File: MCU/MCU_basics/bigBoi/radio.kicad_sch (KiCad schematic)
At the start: 23 parts, among them J1 Conn_Coaxial, U1 SX1276, U2 PE4259, Y1 32MHz

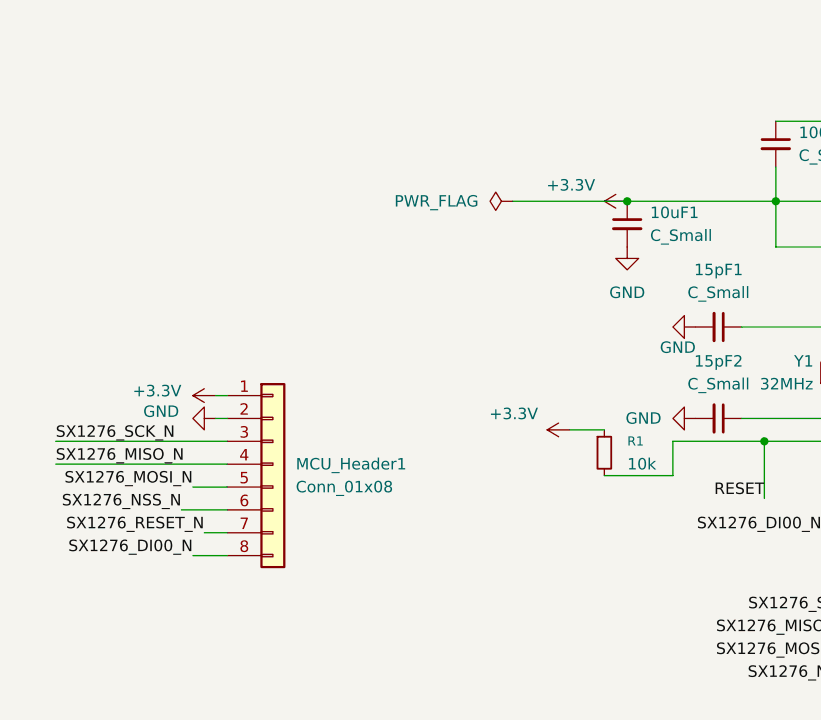
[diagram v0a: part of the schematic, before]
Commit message: Schematic pins assignment
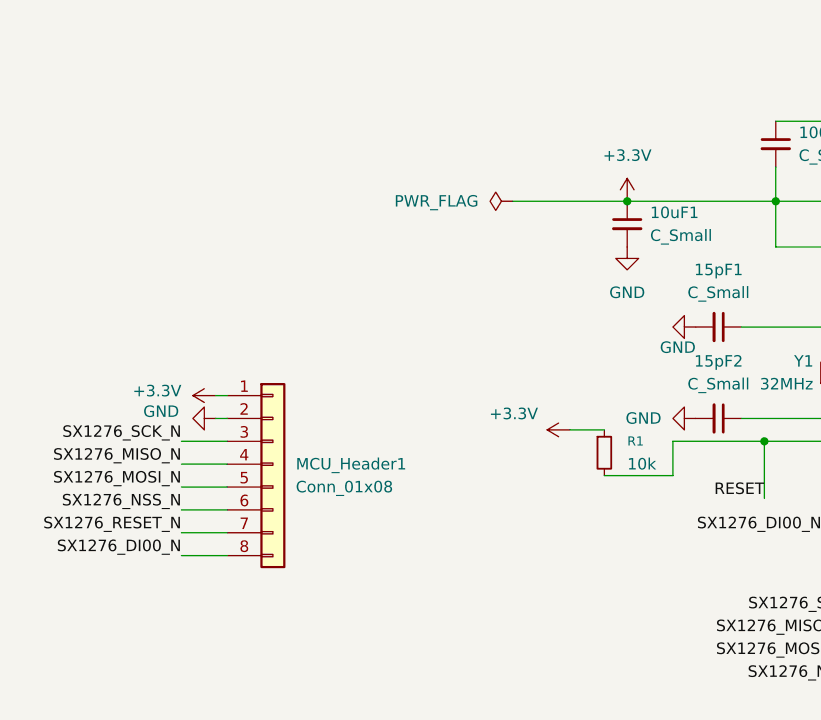
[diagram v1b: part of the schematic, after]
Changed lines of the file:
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@@
 	(wire
 		(pts
-			(xy 48.26 95.25) (xy 52.07 95.25)
+			(xy 46.99 95.25) (xy 52.07 95.25)
 		)
 		(stroke
@@
 	(wire
 		(pts
-			(xy 33.02 92.71) (xy 52.07 92.71)
+			(xy 46.99 92.71) (xy 52.07 92.71)
 		)
 		(stroke
@@
 	(wire
 		(pts
-			(xy 33.02 90.17) (xy 52.07 90.17)
+			(xy 46.99 90.17) (xy 52.07 90.17)
 		)
 		(stroke
@@
 	(wire
 		(pts
-			(xy 48.26 102.87) (xy 52.07 102.87)
+			(xy 46.99 102.87) (xy 52.07 102.87)
 		)
 		(stroke
@@
 	(wire
 		(pts
-			(xy 49.53 100.33) (xy 52.07 100.33)
+			(xy 46.99 100.33) (xy 52.07 100.33)
 		)
 		(stroke
@@
 	)
 	(label "SX1276_MOSI_N"
-		(at 48.26 95.25 180)
+		(at 46.99 95.25 180)
 		(effects
 			(font
@@
 	)
 	(label "SX1276_SCK_N"
-		(at 33.02 90.17 0)
+		(at 46.99 90.17 180)
 		(effects
 			(font
 				(size 1.27 1.27)
 			)
-			(justify left bottom)
+			(justify right bottom)
 		)
 	)
@@
 	)
 	(label "SX1276_DI00_N"
-		(at 48.26 102.87 180)
+		(at 46.99 102.87 180)
 		(effects
 			(font
@@
 	)
 	(label "SX1276_RESET_N"
-		(at 49.53 100.33 180)
+		(at 46.99 100.33 180)
 		(effects
 			(font
@@
 	)
 	(label "SX1276_MISO_N"
-		(at 33.02 92.71 0)
+		(at 46.99 92.71 180)
 		(effects
 			(font
 				(size 1.27 1.27)
 			)
-			(justify left bottom)
+			(justify right bottom)
 		)
 	)
@@
 	)
 	(symbol
+		(lib_id "power:+3.3V")
+		(at 96.52 63.5 0)
+		(unit 1)
+		(body_style 1)
+		(exclude_from_sim no)
+		(in_bom yes)
+		(on_board yes)
+		(in_pos_files yes)
+		(dnp no)
+		(fields_autoplaced yes)
+		(property "Reference" "#PWR057"
+			(at 96.52 67.31 0)
+			(hide yes)
+			(show_name no)
+			(do_not_autoplace no)
+			(effects
+				(font
+					(size 1.27 1.27)
+				)
+			)
+		)
+		(property "Value" "+3.3V"
+			(at 96.52 58.42 0)
+			(show_name no)
+			(do_not_autoplace no)
+			(effects
+				(font
+					(size 1.27 1.27)
+				)
+			)
+		)
+		(property "Footprint" ""
+			(at 96.52 63.5 0)
+			(hide yes)
+			(show_name no)
+			(do_not_autoplace no)
+			(effects
+				(font
+					(size 1.27 1.27)
+				)
+			)
+		)
+		(property "Datasheet" ""
+			(at 96.52 63.5 0)
+			(hide yes)
+			(show_name no)
+			(do_not_autoplace no)
+			(effects
+				(font
+					(size 1.27 1.27)
+				)
+			)
+		)
+		(property "Description" "Power symbol creates a global label with name \"+3.3V\""
+			(at 96.52 63.5 0)
+			(hide yes)
+			(show_name no)
+			(do_not_autoplace no)
+			(effects
+				(font
+					(size 1.27 1.27)
+				)
+			)
+		)
+		(pin "1"
+		)
+		(instances
+			(project "bigBoi"
+				(path "/0a118c22-2522-42a6-b7a6-70c79326ece4/f88a4f50-bdfc-44db-bd06-a2b26240335b"
+					(reference "#PWR057")
+					(unit 1)
+				)
+			)
+		)
+	)
+	(symbol
 		(lib_id "Device:C_Small")
 		(at 191.77 91.44 180)
@@
 					(unit 1)
 				)
-			)
-		)
-	)
-	(symbol
-		(lib_id "power:+3.3V")
-		(at 96.52 63.5 90)
-		(unit 1)
-		(body_style 1)
-		(exclude_from_sim no)
-		(in_bom yes)
-		(on_board yes)
-		(in_pos_files yes)
-		(dnp no)
-		(property "Reference" "#PWR022"
-			(at 100.33 63.5 0)
-			(hide yes)
-			(show_name no)
-			(do_not_autoplace no)
-			(effects
-				(font
-					(size 1.27 1.27)
-				)
-			)
-		)
-		(property "Value" "+3.3V"
-			(at 92.964 61.722 90)
-			(show_name no)
-			(do_not_autoplace no)
-			(effects
-				(font
-					(size 1.27 1.27)
-				)
-				(justify left)
-			)
-		)
-		(property "Footprint" ""
-			(at 96.52 63.5 0)
-			(hide yes)
-			(show_name no)
-			(do_not_autoplace no)
-			(effects
-				(font
-					(size 1.27 1.27)
-				)
-			)
-		)
-		(property "Datasheet" ""
-			(at 96.52 63.5 0)
-			(hide yes)
-			(show_name no)
-			(do_not_autoplace no)
-			(effects
-				(font
-					(size 1.27 1.27)
-				)
-			)
-		)
-		(property "Description" "Power symbol creates a global label with name \"+3.3V\""
-			(at 96.52 63.5 0)
-			(hide yes)
-			(show_name no)
-			(do_not_autoplace no)
-			(effects
-				(font
-					(size 1.27 1.27)
-				)
-			)
-		)
-		(pin "1"
-		)
-		(instances
-			(project "bigBoi"
-				(path "/0a118c22-2522-42a6-b7a6-70c79326ece4/f88a4f50-bdfc-44db-bd06-a2b26240335b"
-					(reference "#PWR022")
-					(unit 1)
-				)

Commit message: schematic connections
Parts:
- renumbered 100nF6 to 100nF5, 100nF5 to 100nF6, 47pF2 to 47pF1, 47pF1 to 47pF2, L3 to L1, L1 to L2, L2 to L3, R1 to R2, U1 to U3, U2 to U4, Y1 to Y2

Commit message: ERC resolving
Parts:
- removed MCU_Header1: Conn_01x08, symbol Connector_Generic:Conn_01x08
- 1.5pF1, 100nF1, 100nF2, 100nF3, 100nF4, 100nF5, 100nF6, 10uF1, 15pF1, 15pF2, 1nF1, 4.7pF1, 47pF1, 47pF2: footprint (none) -> Capacitor_SMD:C_0402_1005Metric
- R2: footprint (none) -> Resistor_SMD:R_0402_1005Metric
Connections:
- net RESET is gone; now on net SX1276_RESET_N: R2.2, U3.7 (~{RESET})

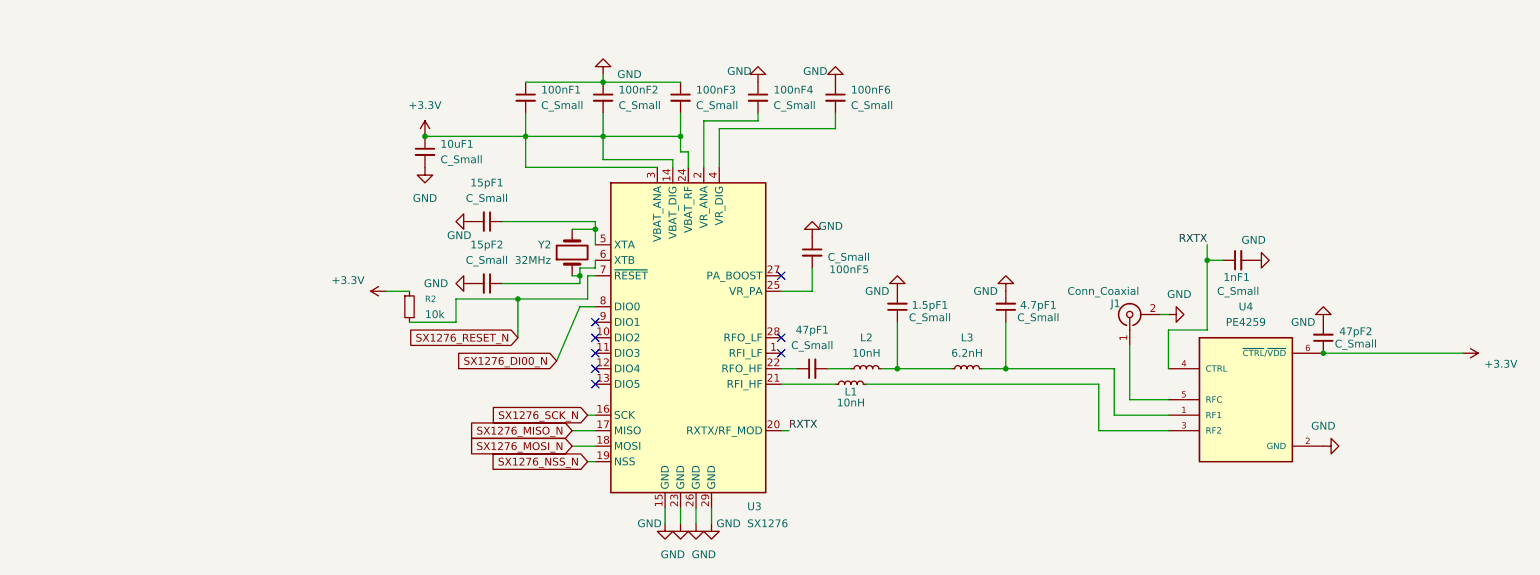
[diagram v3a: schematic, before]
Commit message: most footprints assigned
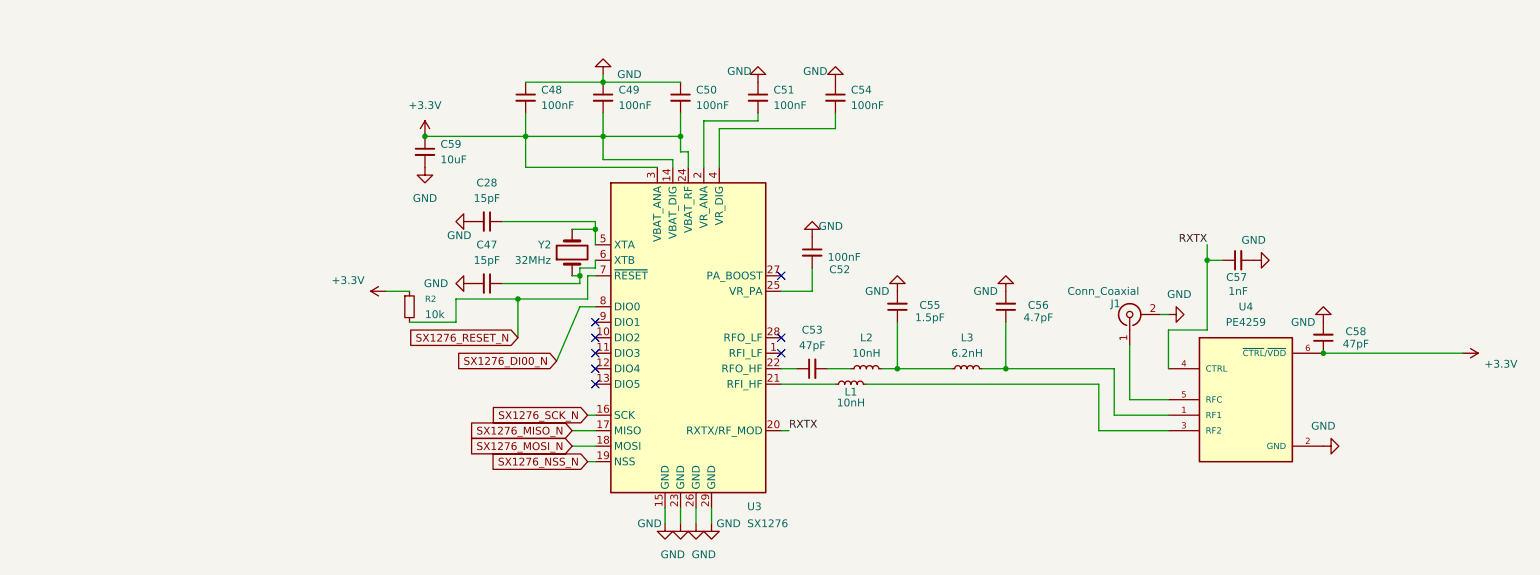
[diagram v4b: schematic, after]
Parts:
- C28: renamed from 15pF1; value C_Small -> 15pF
- C47: renamed from 15pF2; value C_Small -> 15pF
- C48: renamed from 100nF1; value C_Small -> 100nF
- C49: renamed from 100nF2; value C_Small -> 100nF
- C50: renamed from 100nF3; value C_Small -> 100nF
- C51: renamed from 100nF4; value C_Small -> 100nF
- C52: renamed from 100nF5; value C_Small -> 100nF
- C53: renamed from 47pF1; value C_Small -> 47pF
- C54: renamed from 100nF6; value C_Small -> 100nF
- C55: renamed from 1.5pF1; value C_Small -> 1.5pF
- C56: renamed from 4.7pF1; value C_Small -> 4.7pF
- C57: renamed from 1nF1; value C_Small -> 1nF
- C58: renamed from 47pF2; value C_Small -> 47pF
- C59: renamed from 10uF1; value C_Small -> 10uF; footprint Capacitor_SMD:C_0402_1005Metric -> Capacitor_SMD:C_0805_2012Metric
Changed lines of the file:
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@@
 		(dnp no)
 		(fields_autoplaced yes)
-		(property "Reference" "15pF2"
+		(property "Reference" "C47"
 			(at 106.6736 81.28 90)
 			(show_name no)
@@
 			)
 		)
-		(property "Value" "C_Small"
+		(property "Value" "15pF"
 			(at 106.6736 83.82 90)
 			(show_name no)
@@
 			(project "bigBoi"
 				(path "/0a118c22-2522-42a6-b7a6-70c79326ece4/f88a4f50-bdfc-44db-bd06-a2b26240335b"
-					(reference "15pF2")
+					(reference "C47")
 					(unit 1)
 				)
@@
 		(in_pos_files yes)
 		(dnp no)
-		(property "Reference" "47pF2"
+		(property "Reference" "C58"
 			(at 249.174 95.504 0)
 			(show_name no)
@@
 			)
 		)
-		(property "Value" "C_Small"
+		(property "Value" "47pF"
 			(at 249.174 97.536 0)
 			(show_name no)
@@
 			(project "bigBoi"
 				(path "/0a118c22-2522-42a6-b7a6-70c79326ece4/f88a4f50-bdfc-44db-bd06-a2b26240335b"
-					(reference "47pF2")
+					(reference "C58")
 					(unit 1)
 				)
@@
 		(in_pos_files yes)
 		(dnp no)
-		(property "Reference" "100nF5"
+		(property "Reference" "C52"
 			(at 162.814 85.344 0)
 			(show_name no)
@@
 			)
 		)
-		(property "Value" "C_Small"
+		(property "Value" "100nF"
 			(at 162.56 83.312 0)
 			(show_name no)
@@
 			(project "bigBoi"
 				(path "/0a118c22-2522-42a6-b7a6-70c79326ece4/f88a4f50-bdfc-44db-bd06-a2b26240335b"
-					(reference "100nF5")
+					(reference "C52")
 					(unit 1)
 				)
@@
 		(dnp no)
 		(fields_autoplaced yes)
-		(property "Reference" "100nF4"
+		(property "Reference" "C51"
 			(at 153.67 55.8862 0)
 			(show_name no)
@@
 			)
 		)
-		(property "Value" "C_Small"
+		(property "Value" "100nF"
 			(at 153.67 58.4262 0)
 			(show_name no)
@@
 			(project "bigBoi"
 				(path "/0a118c22-2522-42a6-b7a6-70c79326ece4/f88a4f50-bdfc-44db-bd06-a2b26240335b"
-					(reference "100nF4")
+					(reference "C51")
 					(unit 1)
 				)
@@
 		(dnp no)
 		(fields_autoplaced yes)
-		(property "Reference" "47pF1"
+		(property "Reference" "C53"
 			(at 160.0263 95.25 90)
 			(show_name no)
@@
 			)
 		)
-		(property "Value" "C_Small"
+		(property "Value" "47pF"
 			(at 160.0263 97.79 90)
 			(show_name no)
@@
 			(project "bigBoi"
 				(path "/0a118c22-2522-42a6-b7a6-70c79326ece4/f88a4f50-bdfc-44db-bd06-a2b26240335b"
-					(reference "47pF1")
+					(reference "C53")
 					(unit 1)
 				)
@@
 		(dnp no)
 		(fields_autoplaced yes)
-		(property "Reference" "10uF1"
+		(property "Reference" "C59"
 			(at 99.06 64.7762 0)
 			(show_name no)
@@
 			)
 		)
-		(property "Value" "C_Small"
+		(property "Value" "10uF"
 			(at 99.06 67.3162 0)
 			(show_name no)
@@
 			)
 		)
-		(property "Footprint" "Capacitor_SMD:C_0402_1005Metric"
+		(property "Footprint" "Capacitor_SMD:C_0805_2012Metric"
 			(at 96.52 66.04 0)
 			(hide yes)
@@
 			(project "bigBoi"
 				(path "/0a118c22-2522-42a6-b7a6-70c79326ece4/f88a4f50-bdfc-44db-bd06-a2b26240335b"
-					(reference "10uF1")
+					(reference "C59")
 					(unit 1)
 				)
@@
 		(dnp no)
 		(fields_autoplaced yes)
-		(property "Reference" "100nF2"
+		(property "Reference" "C49"
 			(at 128.27 55.8862 0)
 			(show_name no)
@@
 			)
 		)
-		(property "Value" "C_Small"
+		(property "Value" "100nF"
 			(at 128.27 58.4262 0)
 			(show_name no)
@@
 			(project "bigBoi"
 				(path "/0a118c22-2522-42a6-b7a6-70c79326ece4/f88a4f50-bdfc-44db-bd06-a2b26240335b"
-					(reference "100nF2")
+					(reference "C49")
 					(unit 1)
 				)
@@
 		(dnp no)
 		(fields_autoplaced yes)
-		(property "Reference" "100nF1"
+		(property "Reference" "C48"
 			(at 115.57 55.8862 0)
 			(show_name no)
@@
 			)
 		)
-		(property "Value" "C_Small"
+		(property "Value" "100nF"
 			(at 115.57 58.4262 0)
 			(show_name no)
@@
 			(project "bigBoi"
 				(path "/0a118c22-2522-42a6-b7a6-70c79326ece4/f88a4f50-bdfc-44db-bd06-a2b26240335b"
-					(reference "100nF1")
+					(reference "C48")
 					(unit 1)
 				)
@@
 		(dnp no)
 		(fields_autoplaced yes)
-		(property "Reference" "100nF6"
+		(property "Reference" "C54"
 			(at 166.37 55.8862 0)
 			(show_name no)
@@
 			)
 		)
-		(property "Value" "C_Small"
+		(property "Value" "100nF"
 			(at 166.37 58.4262 0)
 			(show_name no)
@@
 			(project "bigBoi"
 				(path "/0a118c22-2522-42a6-b7a6-70c79326ece4/f88a4f50-bdfc-44db-bd06-a2b26240335b"
-					(reference "100nF6")
+					(reference "C54")
 					(unit 1)
 				)
@@
 		(in_pos_files yes)
 		(dnp no)
-		(property "Reference" "4.7pF1"
+		(property "Reference" "C56"
 			(at 197.104 91.186 0)
 			(show_name no)
@@
 			)
 		)
-		(property "Value" "C_Small"
+		(property "Value" "4.7pF"
 			(at 197.104 93.218 0)
 			(show_name no)
@@
 			(project "bigBoi"
 				(path "/0a118c22-2522-42a6-b7a6-70c79326ece4/f88a4f50-bdfc-44db-bd06-a2b26240335b"
-					(reference "4.7pF1")
+					(reference "C56")
 					(unit 1)
 				)
@@
 		(in_pos_files yes)
 		(dnp no)
-		(property "Reference" "1nF1"
+		(property "Reference" "C57"
 			(at 229.616 86.614 90)
 			(show_name no)
@@
 			)
 		)
-		(property "Value" "C_Small"
+		(property "Value" "1nF"
 			(at 229.87 88.9 90)
 			(show_name no)
@@
 			(project "bigBoi"
 				(path "/0a118c22-2522-42a6-b7a6-70c79326ece4/f88a4f50-bdfc-44db-bd06-a2b26240335b"
-					(reference "1nF1")
+					(reference "C57")
 					(unit 1)
 				)
@@
 		(dnp no)
 		(fields_autoplaced yes)
-		(property "Reference" "15pF1"
+		(property "Reference" "C28"
 			(at 106.6736 71.12 90)
 			(show_name no)
@@
 			)
 		)
-		(property "Value" "C_Small"
+		(property "Value" "15pF"
 			(at 106.6736 73.66 90)
 			(show_name no)
@@
 			(project "bigBoi"
 				(path "/0a118c22-2522-42a6-b7a6-70c79326ece4/f88a4f50-bdfc-44db-bd06-a2b26240335b"
-					(reference "15pF1")
+					(reference "C28")
 					(unit 1)
 				)
@@
 		(in_pos_files yes)
 		(dnp no)
-		(property "Reference" "1.5pF1"
+		(property "Reference" "C55"
 			(at 179.324 91.186 0)
 			(show_name no)
@@
 			)
 		)
-		(property "Value" "C_Small"
+		(property "Value" "1.5pF"
 			(at 179.324 93.218 0)
 			(show_name no)
@@
 			(project "bigBoi"
 				(path "/0a118c22-2522-42a6-b7a6-70c79326ece4/f88a4f50-bdfc-44db-bd06-a2b26240335b"
-					(reference "1.5pF1")
+					(reference "C55")
 					(unit 1)
 				)
@@
 		(dnp no)
 		(fields_autoplaced yes)
-		(property "Reference" "100nF3"
+		(property "Reference" "C50"
 			(at 140.97 55.8862 0)
 			(show_name no)
@@
 			)
 		)
-		(property "Value" "C_Small"
+		(property "Value" "100nF"
 			(at 140.97 58.4262 0)
 			(show_name no)
@@
 			(project "bigBoi"
 				(path "/0a118c22-2522-42a6-b7a6-70c79326ece4/f88a4f50-bdfc-44db-bd06-a2b26240335b"
-					(reference "100nF3")
-					(unit 1)
-				)
+					(reference "C50")
+					(unit 1)
+				)

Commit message: small changes
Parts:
- J1: footprint (none) -> Connector_Coaxial:U.FL_Hirose_U.FL-R-SMT-1_Vertical
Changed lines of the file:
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@@
 			)
 		)
-		(property "Footprint" ""
+		(property "Footprint" "Connector_Coaxial:U.FL_Hirose_U.FL-R-SMT-1_Vertical"
 			(at 212.09 92.71 0)
 			(hide yes)

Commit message: Y2 fixed
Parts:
- L1, L2, L3: footprint (none) -> Inductor_SMD:L_0402_1005Metric
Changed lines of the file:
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@@
 			)
 		)
-		(property "Footprint" ""
+		(property "Footprint" "Inductor_SMD:L_0402_1005Metric"
 			(at 185.42 101.6 0)
 			(hide yes)
@@
 			)
 		)
-		(property "Footprint" ""
+		(property "Footprint" "Inductor_SMD:L_0402_1005Metric"
 			(at 168.91 101.6 0)
 			(hide yes)
@@
 			)
 		)
-		(property "Footprint" ""
+		(property "Footprint" "Inductor_SMD:L_0402_1005Metric"
 			(at 166.37 104.14 0)
 			(hide yes)
